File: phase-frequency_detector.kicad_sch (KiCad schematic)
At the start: 63 parts, among them J1 REF, J2 IN, J3 Error_Out, J4 C64AC, U1 HMC439QS16G, U2 LT3045EMSE, U3 LT3094EMSE, U4 ADA4896-2ARMZ, U6 HMC365S8G, U7 L7808

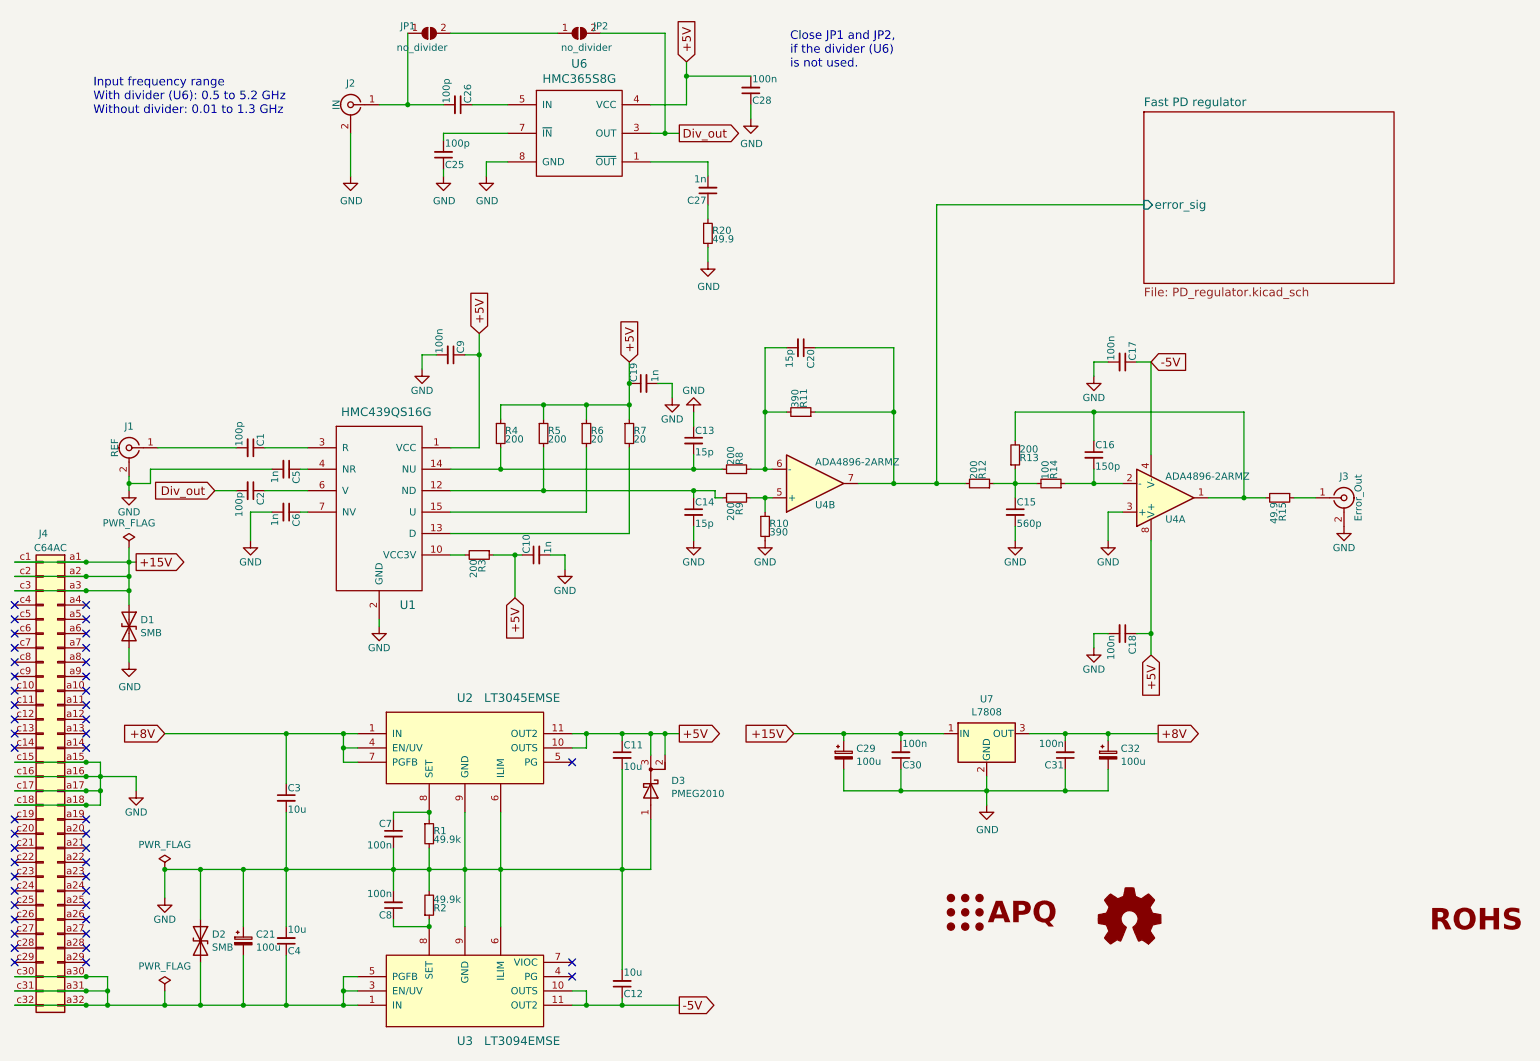
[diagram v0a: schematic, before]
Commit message: Updated to KiCad 7 Added CI pipeline Fixed trailing whitespaces of MFN and PN labels Fixed ERC/DRC errors
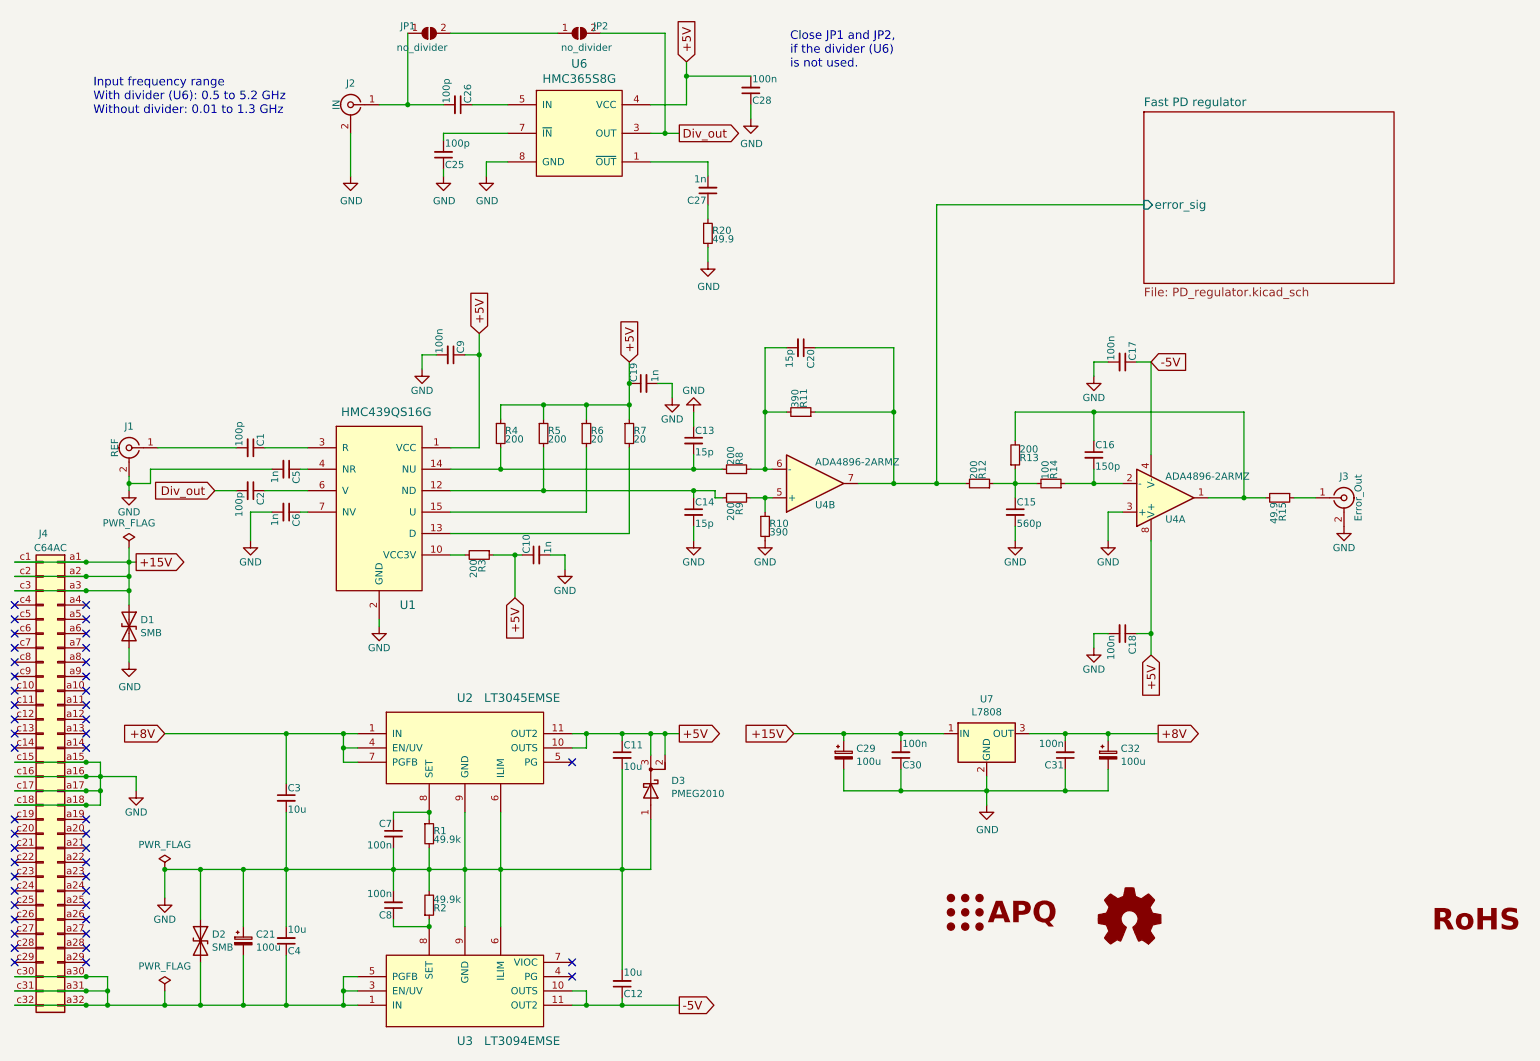
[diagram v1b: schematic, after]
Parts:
- C10, C19, C27, C5, C6: PN C0603X102K4RACAUTO -> C0603X102K4RACAUTO
- C11, C12, C3, C4: PN C3225X7R2A106K250AC -> C3225X7R2A106K250AC
- C13, C14, C20: MFN Vishay / Vitramon -> Vishay / Vitramon; PN VJ0603A150JXBAC -> VJ0603A150JXBAC
- C15: MFN Vishay / Vitramon -> Vishay / Vitramon; PN VJ0603A561JXAAC -> VJ0603A561JXAAC
- C16: MFN Vishay / Vitramon -> Vishay / Vitramon; PN VJ0603A151JXBAC -> VJ0603A151JXBAC
- C17, C18, C28, C30, C31, C9: PN C0603C104K5RAC3121 -> C0603C104K5RAC3121
- C21, C29, C32: PN ECA-1AM101I -> ECA-1AM101I
- J3: MFN Linx Technologies -> Linx Technologies
- LOGO3: symbol Custom_logos:Logo_ROHS -> Custom_logos:Logo_RoHS; now left out of the parts list
- R1, R2: MFN Panasonic -> Panasonic; PN ERJ-UP3F4992V -> ERJ-UP3F4992V
- R15: MFN Vishay / Dale -> Vishay / Dale; PN CRCW121049R9FKEA -> CRCW121049R9FKEA
- R20: PN ERJ-UP3F49R9V -> ERJ-UP3F49R9V
- U6: footprint footprints:SOIC-8-1EP_3.9x4.9mm_P1.27mm_EP2.41x3.81mm_DNF -> Package_SO:SOIC-8-1EP_3.9x4.9mm_P1.27mm_EP2.41x3.81mm
- U7: MFN STMicroelectronics -> STMicroelectronics; PN L7808ABV-DG -> L7808ABV-DG
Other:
- company: Atoms-Photons-Quanta, IAP, TU Darmstadt -> Atoms-Photons-Quanta, Institut für Angewandte Physik, TU Darmstadt

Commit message: Fixed logos on schematic
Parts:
- LOGO1, LOGO2: Config DNF -> (none); now left out of the parts list
- LOGO3: Config DNF -> (none)
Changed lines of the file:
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@@
   )
   (symbol (lib_id "Custom_logos:Logo_APQ") (at 173.99 171.45 0) (unit 1)
-    (in_bom yes) (on_board yes) (dnp no)
+    (in_bom no) (on_board yes) (dnp no)
     (property "Reference" "LOGO1" (at 180.34 164.465 0)
       (effects (font (size 1.27 1.27)) hide)
@@
     )
     (property "Datasheet" "~" (at 181.61 171.45 0)
-      (effects (font (size 1.27 1.27)) hide)
-    )
-    (property "Config" "DNF" (at 173.99 171.45 0)
       (effects (font (size 1.27 1.27)) hide)
     )
@@
   )
   (symbol (lib_id "Graphic:Logo_Open_Hardware_Small") (at 210.82 172.72 0) (unit 1)
-    (in_bom yes) (on_board yes) (dnp no)
+    (in_bom no) (on_board yes) (dnp no)
     (property "Reference" "LOGO2" (at 210.82 165.735 0)
       (effects (font (size 1.27 1.27)) hide)
@@
     )
     (property "Datasheet" "~" (at 210.82 172.72 0)
-      (effects (font (size 1.27 1.27)) hide)
-    )
-    (property "Config" "DNF" (at 210.82 172.72 0)
       (effects (font (size 1.27 1.27)) hide)
     )
@@
       (effects (font (size 1.27 1.27)) hide)
     )
-    (property "Config" "DNF" (at 259.08 172.72 0)
-      (effects (font (size 1.27 1.27)) hide)
-    )

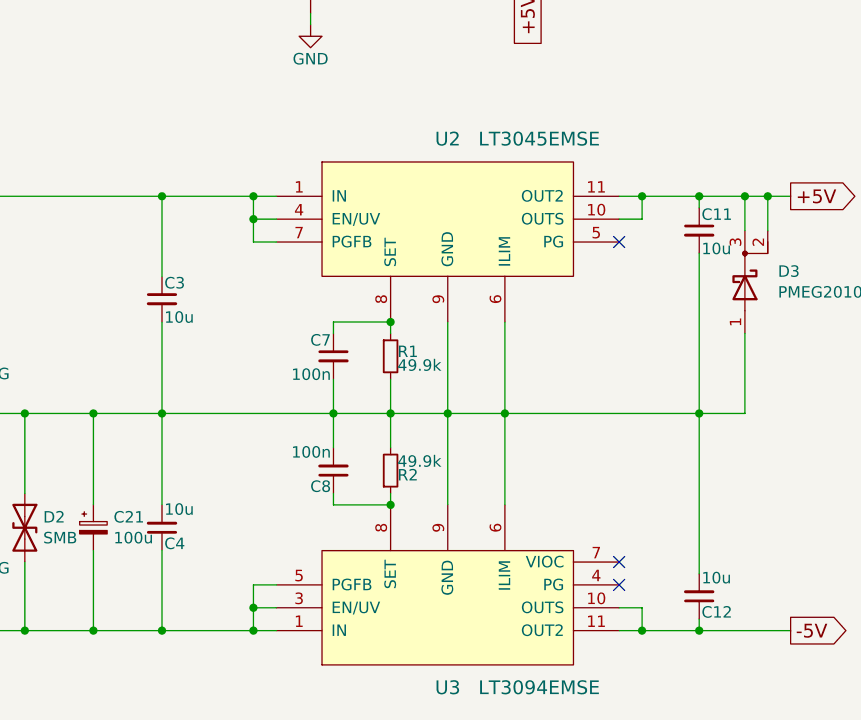
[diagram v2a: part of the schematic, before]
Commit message: Update LT3045/LT3094 symbols
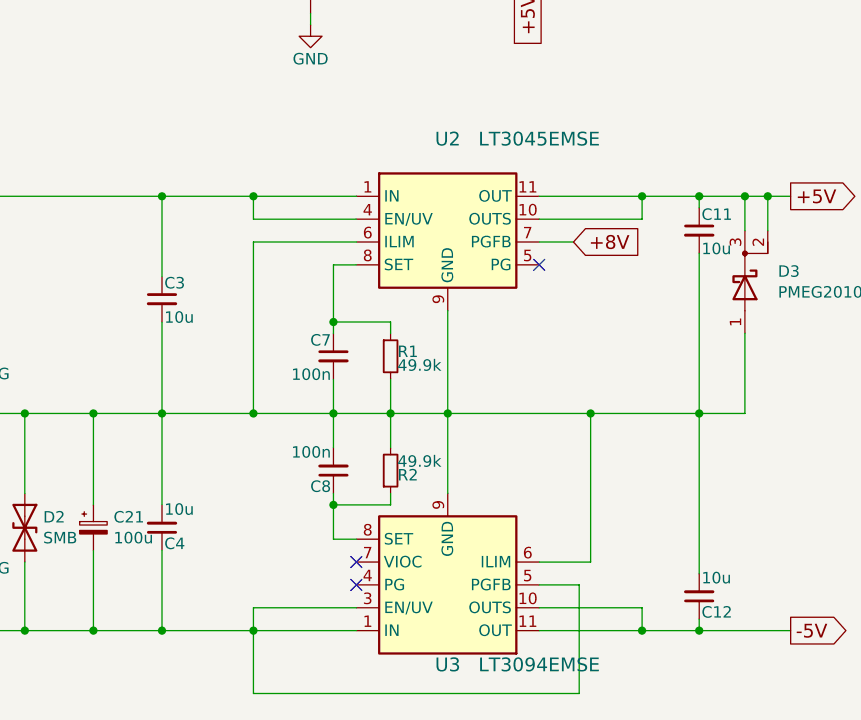
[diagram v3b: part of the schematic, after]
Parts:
- U2: symbol Linear-Technology:LT3045EMSE -> Regulator_Linear:LT3045xMSE
- U3: symbol Linear-Technology:LT3094EMSE -> Regulator_Linear:LT3094xMSE
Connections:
- net IN: no longer names the net of C21.2, C4.1, D2.2 (A2), J4.a30 (Pin_a30), J4.a31 (Pin_a31), J4.a32 (Pin_a32), J4.c30 (Pin_c30), J4.c31 (Pin_c31), J4.c32 (Pin_c32), U3.1 (IN), U3.13 (IN), U3.2 (IN), U3.3 (EN/UV), U3.5 (PGFB)
- net IN2 renamed +8V
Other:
- moved on the sheet: U3
